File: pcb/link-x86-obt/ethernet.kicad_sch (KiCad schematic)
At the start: 35 parts, among them IC24 ENC28J60-I_SO, J6 74990101241, Y1 25MHz

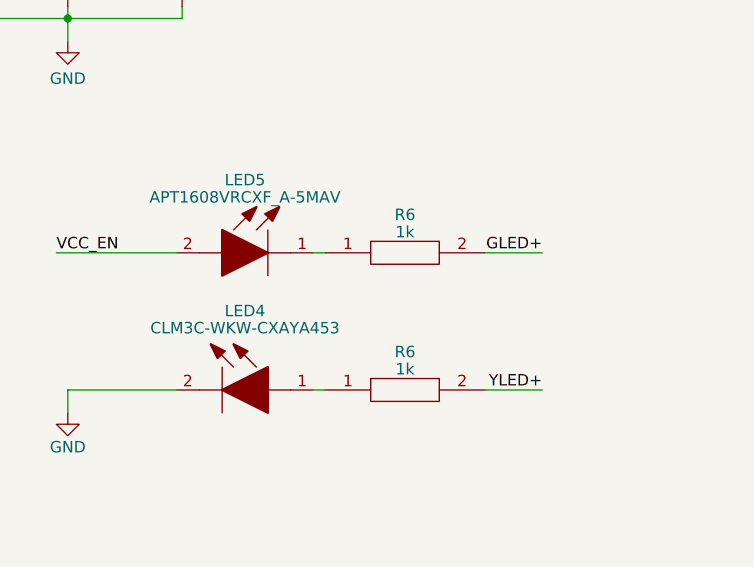
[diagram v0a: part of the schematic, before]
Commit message: add P-channel mosfet to 5VSB line
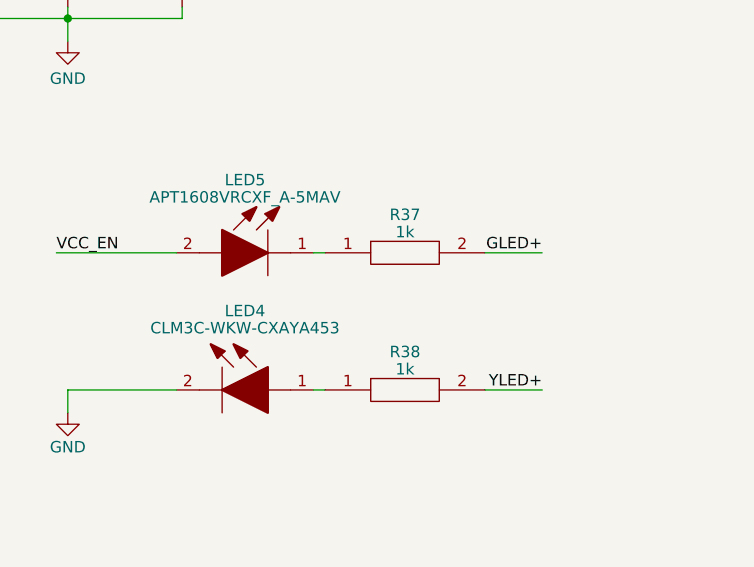
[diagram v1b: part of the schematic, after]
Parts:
- renumbered R6 to R37, R6 to R38

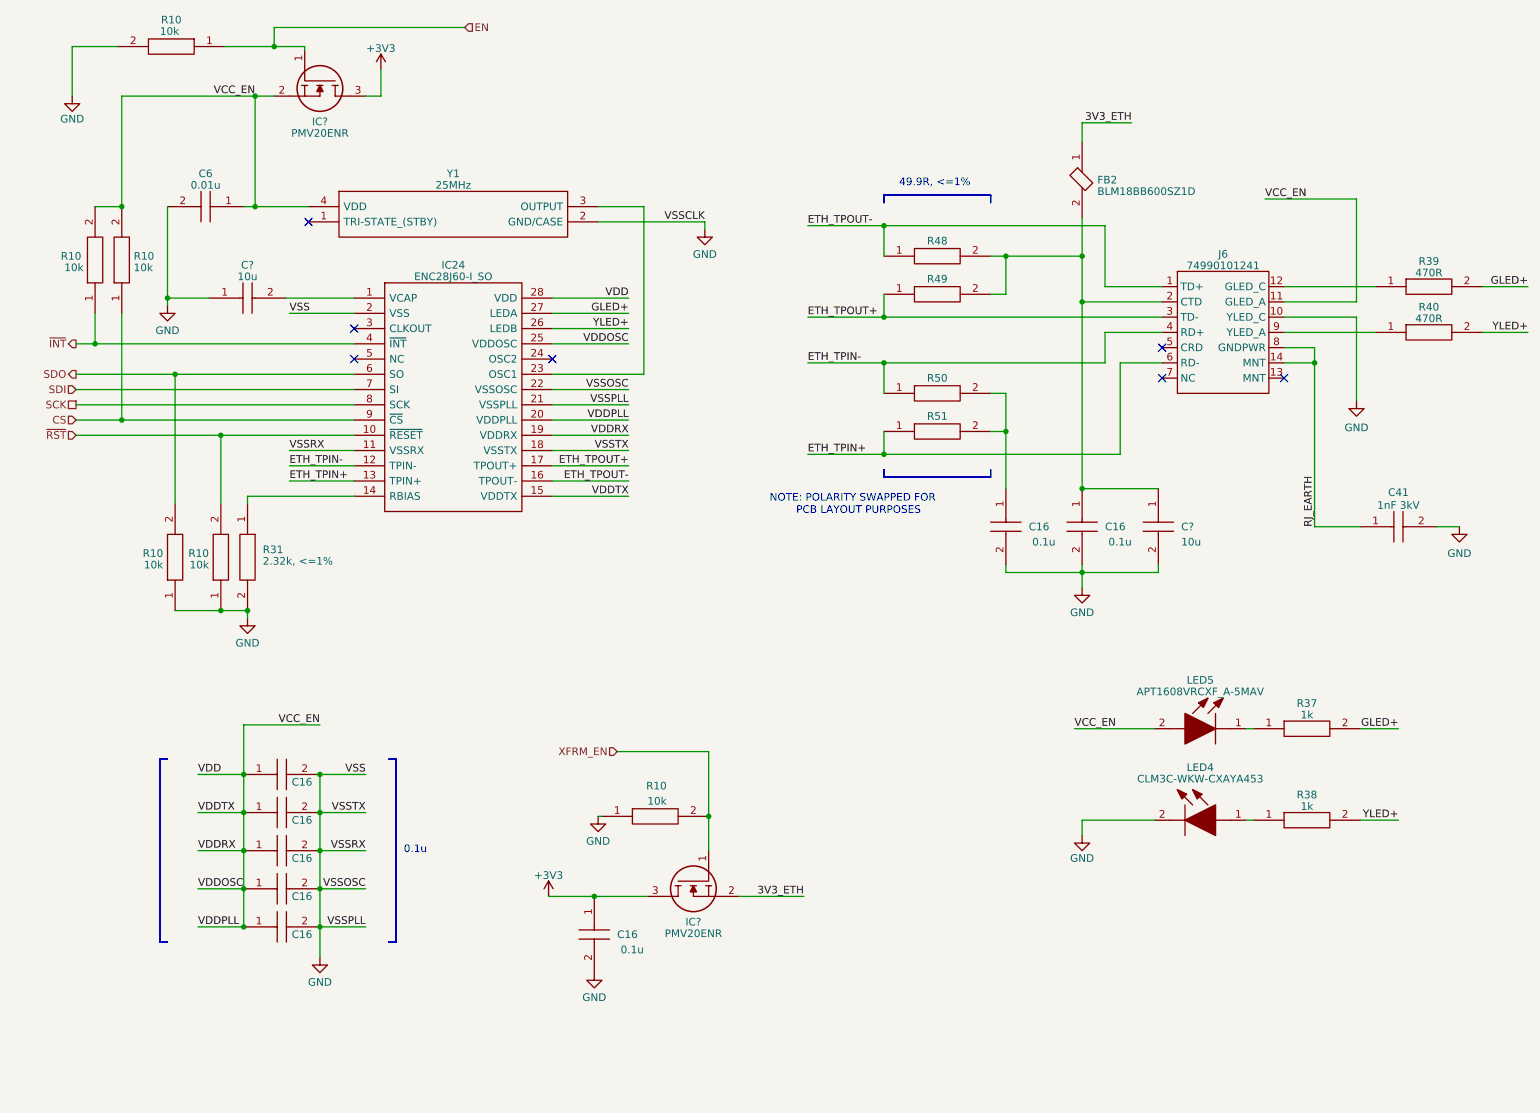
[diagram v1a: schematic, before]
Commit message: omit ethernet enable mosfets in lieu of reset mosfet
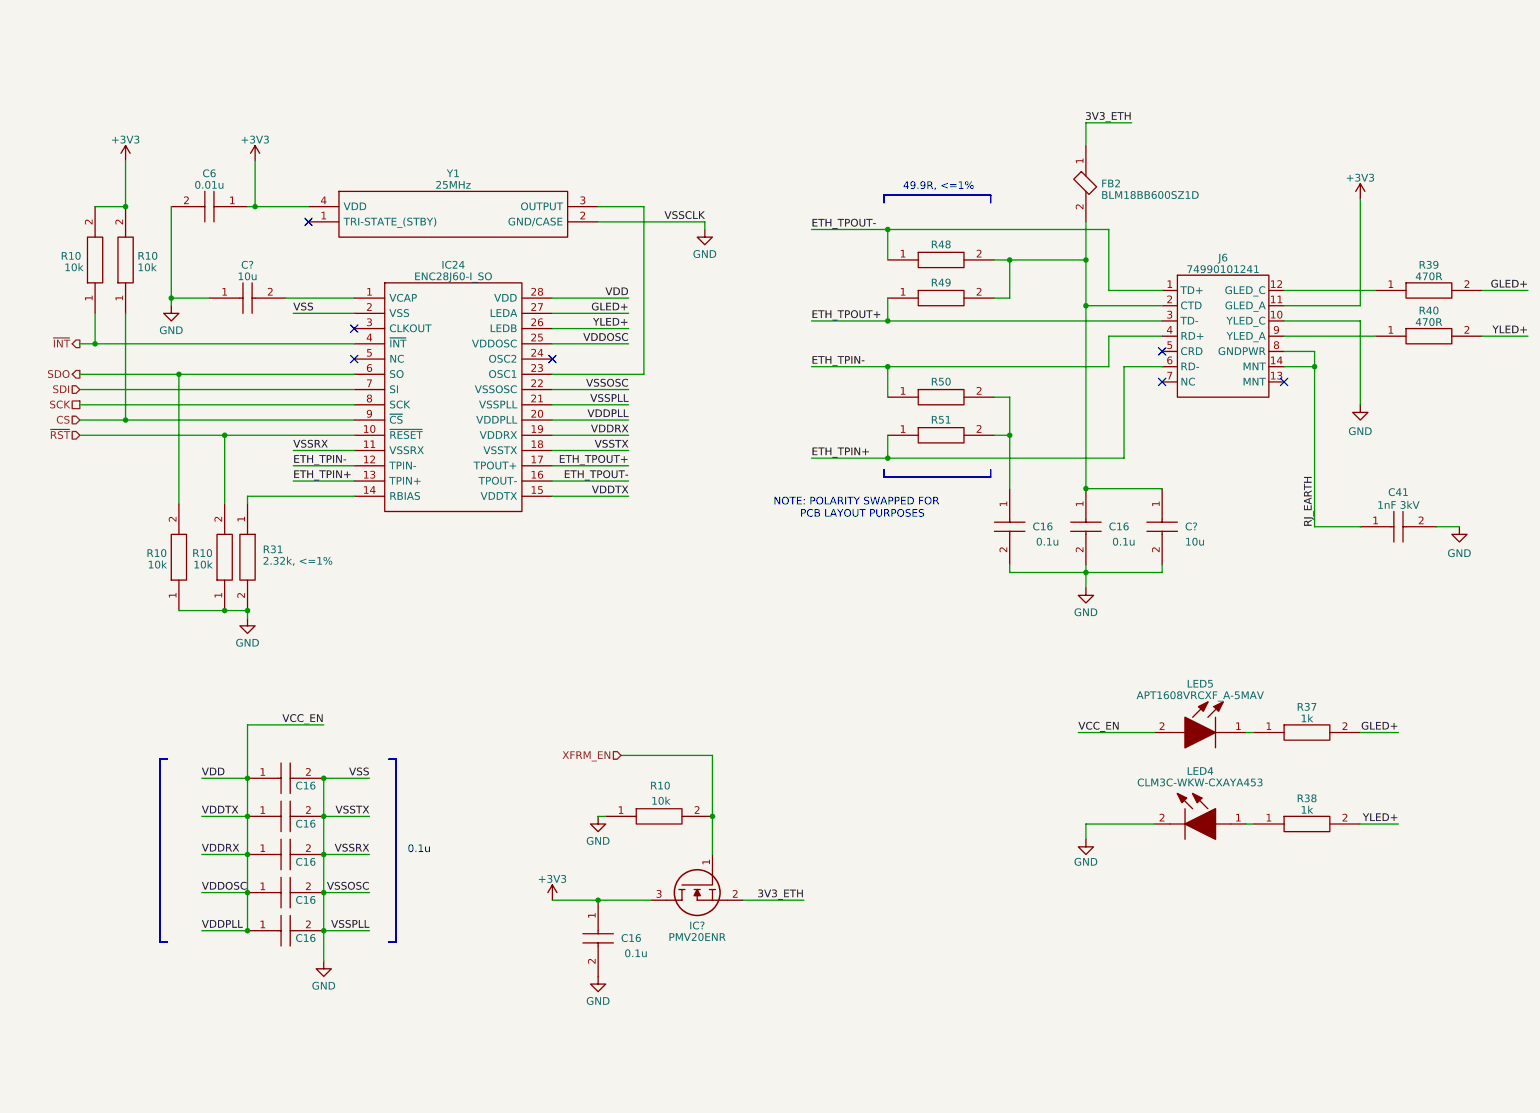
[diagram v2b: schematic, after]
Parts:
- removed IC?: PMV20ENR, SamacSys_Parts:SOT95P230X110-3N, symbol SamacSys_Parts:CSD13380F3T
- removed R10: 10k, RESC1005X40N, symbol SamacSys_Parts:RK73H1ETTP1002F
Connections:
- net +3V3: now also C6.1, J6.11 (GLED_A), R10.2, R10.2, Y1.4 (VDD)
- net VCC_EN: no longer C6.1, J6.11 (GLED_A), R10.2, R10.2, Y1.4 (VDD)
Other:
- moved on the sheet: C16, C6, C?, FB2, IC?, J6, LED4, LED5, R10, R37, R38, R39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

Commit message: initial w5500 schematic (closes #49)
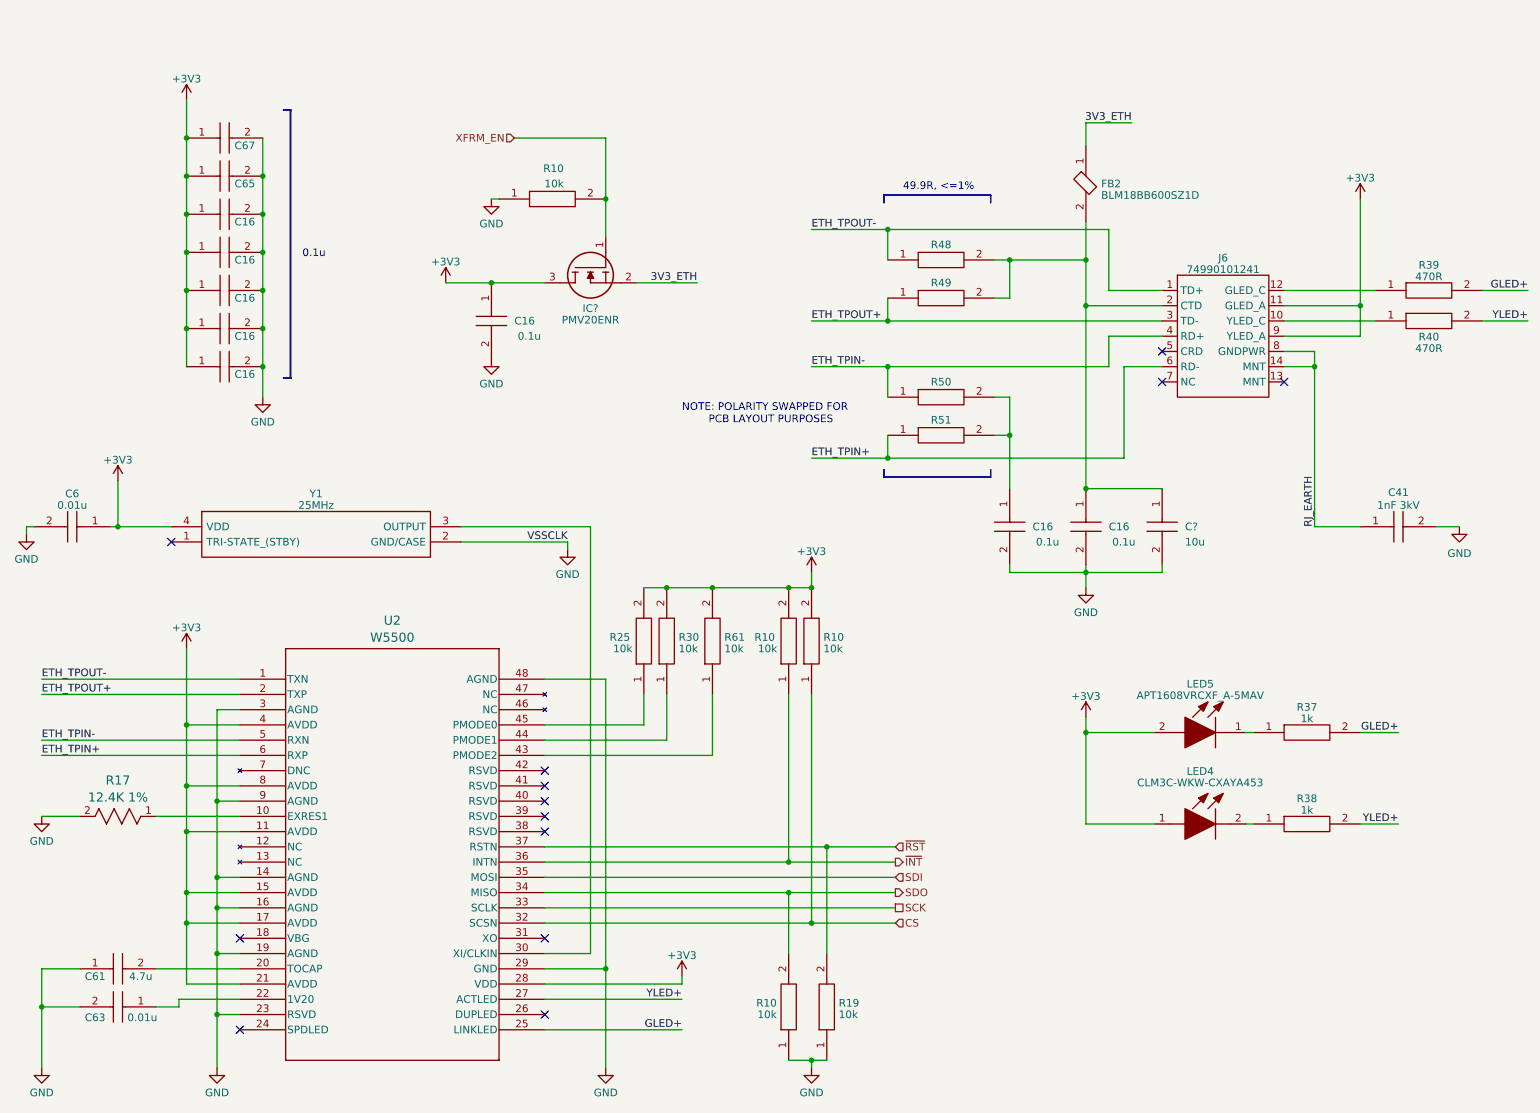
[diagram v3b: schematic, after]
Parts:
- removed C?: 10u, SamacSys_Parts:CAPC2012X135N, symbol SamacSys_Parts:LMK212ABJ106KG8T
- removed IC24: ENC28J60-I_SO, SOIC127P1030X265-28N, symbol SamacSys_Parts:ENC28J60-I_SO
- removed R10: 10k, RESC1005X40N, symbol SamacSys_Parts:RK73H1ETTP1002F
- removed R31: 2.32k, <=1%, SamacSys_Parts:ERJP06__0805_, symbol SamacSys_Parts:ERJ-P06F2321V
- added C61: 4.7u, SamacSys_Parts:CAPC2012X135N, symbol SamacSys_Parts:CL21A475KOFNNNE
- added C63: 0.01u, SamacSys_Parts:CAPC2012X75N, symbol SamacSys_Parts:CL21B103KBANNNC
- added C65, C67: 0.1u, CAPC1005X33N, symbol Oro:MSAST1L3YB5104KFNA01
- added R17: 12.4K 1%, Oro:RES_CRCW_0402, symbol Oro:CRCW040212K4FKED
- added R19, R25, R30, R61: 10k, RESC1005X40N, symbol SamacSys_Parts:RK73H1ETTP1002F
- added U2: W5500, Oro:48LQFP_W5500_WIZ, symbol Oro:W5500
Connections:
- net VCC_EN is gone; now on net +3V3: C16.1, C16.1, C16.1, C16.1, C16.1, LED5.2
- net +3V3: now also J6.9 (YLED_A), LED4.1, C65.1, C67.1, R25.2, R30.2, R61.2, U2.11 (AVDD), U2.15 (AVDD), U2.17 (AVDD), U2.21 (AVDD), U2.28 (VDD), U2.4 (AVDD), U2.8 (AVDD)
- net CS: now also U2.32 (SCSN)
- net ETH_TPIN+: now also U2.6 (RXP)
- net ETH_TPIN-: now also U2.5 (RXN)
- net ETH_TPOUT+: now also U2.2 (TXP)
- net ETH_TPOUT-: now also U2.1 (TXN)
- net GLED+: now also U2.25 (LINKLED)
- net GND: now also C61.1, C63.2, C65.2, C67.2, R17.2, R19.1, U2.14 (AGND), U2.16 (AGND), U2.19 (AGND), U2.23 (RSVD), U2.29 (GND), U2.3 (AGND), U2.48 (AGND), U2.9 (AGND); no longer J6.10 (YLED_C), LED4.2
- net SCK: now also U2.33 (SCLK)
- net SDI: now also U2.35 (MOSI)
- net SDO: now also U2.34 (MISO)
- net YLED+: now also U2.27 (ACTLED)
- net ~{INT}: now also U2.36 (INTN)
- net ~{RST}: now also R19.2, U2.37 (RSTN)
- net at R38.1: now also LED4.2; no longer LED4.1
- net at Y1.3 (OUTPUT): now also U2.30 (XI/CLKIN)
- net at R40.1: now also J6.10 (YLED_C); no longer J6.9 (YLED_A)
- new net: C63.1, U2.22 (1V20)
- new net: C61.2, U2.20 (TOCAP)
- new net: R61.1, U2.43 (PMODE2)
- new net: R17.1, U2.10 (EXRES1)
- new net: R30.1, U2.44 (PMODE1)
- new net: R25.1, U2.45 (PMODE0)
- no-connect marks 7 -> 13
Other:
- moved on the sheet: C16, C6, IC?, R10, R40, Y1

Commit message: rev 7 manufacture candidate
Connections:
- net ETH_TPIN+: now also J6.1 (TD+), R48.1; no longer J6.6 (RD-), R51.1
- net ETH_TPIN-: now also J6.3 (TD-), R49.1; no longer J6.4 (RD+), R50.1
- net ETH_TPOUT+: now also J6.4 (RD+), R50.1; no longer J6.3 (TD-), R49.1
- net ETH_TPOUT-: now also J6.6 (RD-), R51.1; no longer J6.1 (TD+), R48.1
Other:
- note added: "NOTE: RX/TX SWAPPED FOR PCB LAYOUT PURPOSES"
- note removed: "NOTE: POLARITY SWAPPED FOR PCB LAYOUT PURPOSES"
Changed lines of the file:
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@@
 	(title_block
 		(title "Oro Link")
-		(date "2023-07-15")
-		(rev "6")
+		(date "2024-06-09")
+		(rev "7")
 		(company "Oro Operating System")
 		(comment 1 "://oro.sh")
@@
 		)
 	)
-	(text "NOTE: POLARITY SWAPPED FOR\n        PCB LAYOUT PURPOSES"
+	(text "NOTE: RX/TX SWAPPED FOR\n       PCB LAYOUT PURPOSES"
 		(exclude_from_sim no)
-		(at 133.35 83.312 0)
+		(at 125.222 83.566 0)
 		(effects
 			(font
@@
 	)
 	(label "ETH_TPOUT-"
-		(at 154.94 50.8 0)
+		(at 154.94 88.9 0)
 		(fields_autoplaced yes)
 		(effects
@@
 	)
 	(label "ETH_TPIN-"
-		(at 154.94 73.66 0)
+		(at 154.94 66.04 0)
 		(fields_autoplaced yes)
 		(effects
@@
 	)
 	(label "ETH_TPIN+"
-		(at 154.94 88.9 0)
+		(at 154.94 50.8 0)
 		(fields_autoplaced yes)
 		(effects
@@
 	)
 	(label "ETH_TPOUT+"
-		(at 154.94 66.04 0)
+		(at 154.94 73.66 0)
 		(fields_autoplaced yes)
 		(effects
